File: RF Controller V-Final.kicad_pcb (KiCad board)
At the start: 2 copper layers, 132 x 67.5 mm, 41 parts, among them J2 J_OLED, J3 BAT+, J4 BAT-, SW1 EG1218, U1 Teensy4.0, U3 NRF24L01, U5 AP2112K-3.3, U7 Pitch/Roll, U8 TPS542025DDCR, U9 Throttle/Yaw

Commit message: Modified traces
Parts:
- moved U7 4.00 mm to (167.0, 131.0)
- moved U9 4.00 mm to (129.0, 105.0)
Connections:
- SW1 pad 1: /VBAT -> unconnected-(SW1-A-Pad1)
- SW1 pad 3: unconnected-(SW1-C-Pad3) -> /VBAT
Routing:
- net /3v3: track 57.0 -> 63.7 mm
- net /VBAT: track 8.74 -> 15.4 mm
- net /D9: track 47.0 -> 42.3 mm
- net /ADC3: track 65.9 -> 70.2 mm
- net /D10: track 52.3 -> 56.3 mm
- net /ADC0: track 59.1 -> 55.1 mm
- net /ADC1: track 59.9 -> 58.5 mm
- net /ADC2: track 77.9 -> 79.2 mm, vias 2 -> 4

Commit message: Added labels
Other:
- board text added: "5V"
- board text added: "GND"
- board text added: "SW"
- board text added: "VRx"
- board text added: "VRy"
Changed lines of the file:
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@@
+		)
+	)
+	(gr_text "VRx"
+		(at 137.5 118.5 0)
+		(layer "F.SilkS")
+		(effects
+			(font
+				(size 1 1)
+				(thickness 0.1)
+			)
+			(justify left bottom)
+		)
+	)
+	(gr_text "GND"
+		(at 137.5 123.5 0)
+		(layer "F.SilkS")
+		(effects
+			(font
+				(size 1 1)
+				(thickness 0.1)
+			)
+			(justify left bottom)
+		)
+	)
+	(gr_text "VRy"
+		(at 138 116 0)
+		(layer "F.SilkS")
+		(effects
+			(font
+				(size 1 1)
+				(thickness 0.1)
+			)
+			(justify left bottom)
+		)
+	)
+	(gr_text "SW"
+		(at 138.5 113.5 0)
+		(layer "F.SilkS")
+		(effects
+			(font
+				(size 1 1)
+				(thickness 0.1)
+			)
+			(justify left bottom)
+		)
+	)
+	(gr_text "5V"
+		(at 138.5 121 0)
+		(layer "F.SilkS")
+		(effects
+			(font
+				(size 1 1)
+				(thickness 0.1)
+			)
+			(justify left bottom)
+		)
+	)
+	(gr_text "GND"
+		(at 155.5 113.5 0)
+		(layer "F.SilkS")
+		(effects
+			(font
+				(size 1 1)
+				(thickness 0.1)
+			)
+			(justify left bottom)
+		)
+	)
+	(gr_text "5V"
+		(at 155.5 116 0)
+		(layer "F.SilkS")
+		(effects
+			(font
+				(size 1 1)
+				(thickness 0.1)
+			)
+			(justify left bottom)
+		)
+	)
+	(gr_text "VRx"
+		(at 155.5 118.5 0)
+		(layer "F.SilkS")
+		(effects
+			(font
+				(size 1 1)
+				(thickness 0.1)
+			)
+			(justify left bottom)
+		)
+	)
+	(gr_text "VRy"
+		(at 155.5 121 0)
+		(layer "F.SilkS")
+		(effects
+			(font
+				(size 1 1)
+				(thickness 0.1)
+			)
+			(justify left bottom)
+		)
+	)
+	(gr_text "SW"
+		(at 155.5 123.5 0)
+		(layer "F.SilkS")
+		(effects
+			(font
+				(size 1 1)
+				(thickness 0.1)
+			)
+			(justify left bottom)
 		)
 	)

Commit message: Made some design changes
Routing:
- net /D9: track 42.3 -> 43.0 mm, vias 1 -> 2
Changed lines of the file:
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@@
+	)
+	(segment
+		(start 140.039265 112.800735)
+		(end 141.730735 112.800735)
+		(width 0.2)
+		(layer "F.Cu")
+		(net "/D9")
 	)
 	(segment
@@
 	)
 	(segment
+		(start 141.730735 112.800735)
+		(end 141.85 112.92)
+		(width 0.2)
+		(layer "F.Cu")
+		(net "/D9")
+	)
+	(segment
 		(start 107 105.5)
 		(end 105.31 103.81)
@@
 		(net "/D9")
 	)
-	(segment
-		(start 114.42 112.92)
-		(end 141.08 112.92)
-		(width 0.2)
-		(layer "B.Cu")
+	(via
+		(at 140.039265 112.800735)
+		(size 0.6)
+		(drill 0.3)
+		(layers "F.Cu" "B.Cu")
 		(net "/D9")
 	)
 	(segment
+		(start 114 112.5)
+		(end 139.73853 112.5)
+		(width 0.2)
+		(layer "B.Cu")
+		(net "/D9")
+	)
+	(segment
 		(start 107 105.5)
-		(end 114.42 112.92)
+		(end 114 112.5)
+		(width 0.2)
+		(layer "B.Cu")
+		(net "/D9")
+	)
+	(segment
+		(start 139.73853 112.5)
+		(end 140.039265 112.800735)
 		(width 0.2)
 		(layer "B.Cu")
@@
 		(polygon
 			(pts
-				(xy 211.5 68) (xy 214 71) (xy 214 132.5) (xy 211 135.5) (xy 85 135.5) (xy 82 133.5) (xy 82 70.5)
-				(xy 85 68)
+				(xy 82 70.5) (xy 85 68) (xy 211.5 68) (xy 214 71) (xy 214 132.5) (xy 211.5 135.5) (xy 85 135.5)
+				(xy 82 133)
 			)
 		)

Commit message: Added dragon logo
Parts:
- removed the ? at (210.0, 72.0)
- removed the ? at (86.0, 131.5)
- removed the ? at (209.5, 132.0)
- removed the ? at (86.5, 71.5)
- added ?: LOGO, RF_MountingHoles:dragonart, F.Cu at (148.5, 101.0)

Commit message: Edited positions
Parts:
- moved U9 0.50 mm to (129.5, 105.0)
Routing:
- net /D9: track 43.0 -> 44.0 mm
- net /3v3: track 63.7 -> 63.2 mm
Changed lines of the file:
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@@
 	(footprint "JOYYFOOT:JOY1"
 		(layer "F.Cu")
-		(at 129 105 180)
+		(at 129.5 105 180)
 		(property "Reference" "U9"
 			(at 10.73 -10.66 180)
@@
 	)
 	(segment
-		(start 140.039265 112.800735)
-		(end 141.730735 112.800735)
+		(start 142.35 112.92)
+		(end 141.85 112.92)
+		(width 0.2)
+		(layer "F.Cu")
+		(net "/D9")
+	)
+	(segment
+		(start 142.230735 112.800735)
+		(end 142.35 112.92)
 		(width 0.2)
 		(layer "F.Cu")
@@
 	)
 	(segment
-		(start 141.730735 112.800735)
-		(end 141.85 112.92)
+		(start 140.039265 112.800735)
+		(end 142.230735 112.800735)
 		(width 0.2)
 		(layer "F.Cu")
@@
 	)
 	(segment
-		(start 151.55 114.06)
-		(end 145.07 120.54)
-		(width 0.8)
-		(layer "F.Cu")
-		(net "/3v3")
-	)
-	(segment
 		(start 151.55 111.1125)
 		(end 129.9375 89.5)
@@
 	)
 	(segment
-		(start 145.07 120.54)
-		(end 141.85 120.54)
+		(start 151.55 114.06)
+		(end 145.07 120.54)
 		(width 0.8)
 		(layer "F.Cu")
@@
 	)
 	(segment
+		(start 145.07 120.54)
+		(end 142.35 120.54)
+		(width 0.8)
+		(layer "F.Cu")
+		(net "/3v3")
+	)
+	(segment
 		(start 119.66 85.84)
 		(end 118.01 85.84)
@@
 	)
 	(segment
-		(start 128 118)
-		(end 141.85 118)
+		(start 114.31 87)
+		(end 112.754365 87)
 		(width 0.2)
 		(layer "F.Cu")
@@
 	)
 	(segment
-		(start 112.754365 87)
-		(end 114.31 87)
+		(start 111.83 87.924365)
+		(end 111.83 101.83)
 		(width 0.2)
 		(layer "F.Cu")
@@
 	)
 	(segment
-		(start 111.83 87.924365)
-		(end 112.754365 87)
+		(start 115.47 85.84)
+		(end 114.31 87)
 		(width 0.2)
 		(layer "F.Cu")
@@
 	)
 	(segment
-		(start 111.83 101.83)
-		(end 111.83 87.924365)
+		(start 128 118)
+		(end 142.35 118)
 		(width 0.2)
 		(layer "F.Cu")
@@
 	)
 	(segment
-		(start 114.31 87)
-		(end 115.47 85.84)
+		(start 112.754365 87)
+		(end 111.83 87.924365)
 		(width 0.2)
 		(layer "F.Cu")
@@
 	)
 	(segment
-		(start 128 118)
-		(end 111.83 101.83)
+		(start 111.83 101.83)
+		(end 128 118)
 		(width 0.2)
 		(layer "F.Cu")
@@
 	)
 	(segment
-		(start 116.57 85.384365)
-		(end 116.57 96.115635)
+		(start 127.711471 97.44)
+		(end 130.751471 94.4)
 		(width 0.2)
 		(layer "F.Cu")
@@
 	(segment
 		(start 139.1 112.71)
-		(end 141.85 115.46)
+		(end 141.545 115.155)
 		(width 0.2)
 		(layer "F.Cu")
@@
 	)
 	(segment
-		(start 114.03 84.74)
-		(end 115.925635 84.74)
+		(start 139.1 100.251471)
+		(end 139.1 112.71)
 		(width 0.2)
 		(layer "F.Cu")
@@
 	)
 	(segment
-		(start 141.85 115.155)
-		(end 141.85 115.46)
+		(start 141.545 115.155)
+		(end 141.85 115.155)
 		(width 0.2)
 		(layer "F.Cu")
@@
 	)
 	(segment
-		(start 117.894365 97.44)
-		(end 127.711471 97.44)
+		(start 133.248529 94.4)
+		(end 139.1 100.251471)
 		(width 0.2)
 		(layer "F.Cu")
@@
 	)
 	(segment
-		(start 116.57 96.115635)
-		(end 117.894365 97.44)
+		(start 114.03 84.74)
+		(end 115.925635 84.74)
 		(width 0.2)
 		(layer "F.Cu")
@@
 	)
 	(segment
-		(start 127.711471 97.44)
-		(end 130.751471 94.4)
+		(start 115.925635 84.74)
+		(end 116.57 85.384365)
 		(width 0.2)
 		(layer "F.Cu")
@@
 	)
 	(segment
-		(start 139.1 100.251471)
-		(end 139.1 112.71)
+		(start 116.57 85.384365)
+		(end 116.57 96.115635)
 		(width 0.2)
 		(layer "F.Cu")
@@
 	)
 	(segment
-		(start 115.925635 84.74)
-		(end 116.57 85.384365)
+		(start 117.894365 97.44)
+		(end 127.711471 97.44)
 		(width 0.2)
 		(layer "F.Cu")
@@
 	)
 	(segment
-		(start 133.248529 94.4)
-		(end 139.1 100.251471)
+		(start 116.57 96.115635)
+		(end 117.894365 97.44)
 		(width 0.2)
 		(layer "F.Cu")
@@
 	)
 	(segment
-		(start 129.734365 121.98)
-		(end 108.95 101.195635)
+		(start 107.85 85.84)
+		(end 108.95 86.94)
 		(width 0.2)
 		(layer "F.Cu")
@@
 	)
 	(segment
-		(start 154.15 120.54)
-		(end 150.15 120.54)
+		(start 108.95 86.94)
+		(end 108.95 101.195635)
 		(width 0.2)
 		(layer "F.Cu")
@@
 	)
 	(segment
-		(start 142.97 122)
-		(end 142.95 121.98)
+		(start 150.15 120.54)
+		(end 154.15 120.54)
 		(width 0.2)
 		(layer "F.Cu")
@@
 	)
 	(segment
-		(start 108.95 86.94)
-		(end 107.85 85.84)
+		(start 130.474365 121.64)
+		(end 149.05 121.64)
 		(width 0.2)
 		(layer "F.Cu")
@@
 	)
 	(segment
-		(start 150.15 120.54)
-		(end 148.69 122)
+		(start 129.754365 122)
+		(end 130.114365 122)
 		(width 0.2)
 		(layer "F.Cu")
@@
 	)
 	(segment
-		(start 142.95 121.98)
-		(end 129.734365 121.98)
+		(start 149.05 121.64)
+		(end 150.15 120.54)
 		(width 0.2)
 		(layer "F.Cu")
@@
 	(segment
 		(start 108.95 101.195635)
-		(end 108.95 86.94)
+		(end 129.754365 122)
 		(width 0.2)
 		(layer "F.Cu")
@@
 	)
 	(segment
-		(start 148.69 122)
-		(end 142.97 122)
+		(start 130.114365 122)
+		(end 130.474365 121.64)
 		(width 0.2)
 		(layer "F.Cu")
@@
 		(polygon
 			(pts
-				(xy 82 70.5) (xy 85 68) (xy 211.5 68) (xy 214 71) (xy 214 132.5) (xy 211.5 135.5) (xy 85 135.5)
-				(xy 82 133)
+				(xy 82 70.5) (xy 85 68) (xy 211.5 68) (xy 214 71) (xy 214 133) (xy 211.5 135.5) (xy 85.5 135.5)
+				(xy 82 132.5)
 			)
 		)

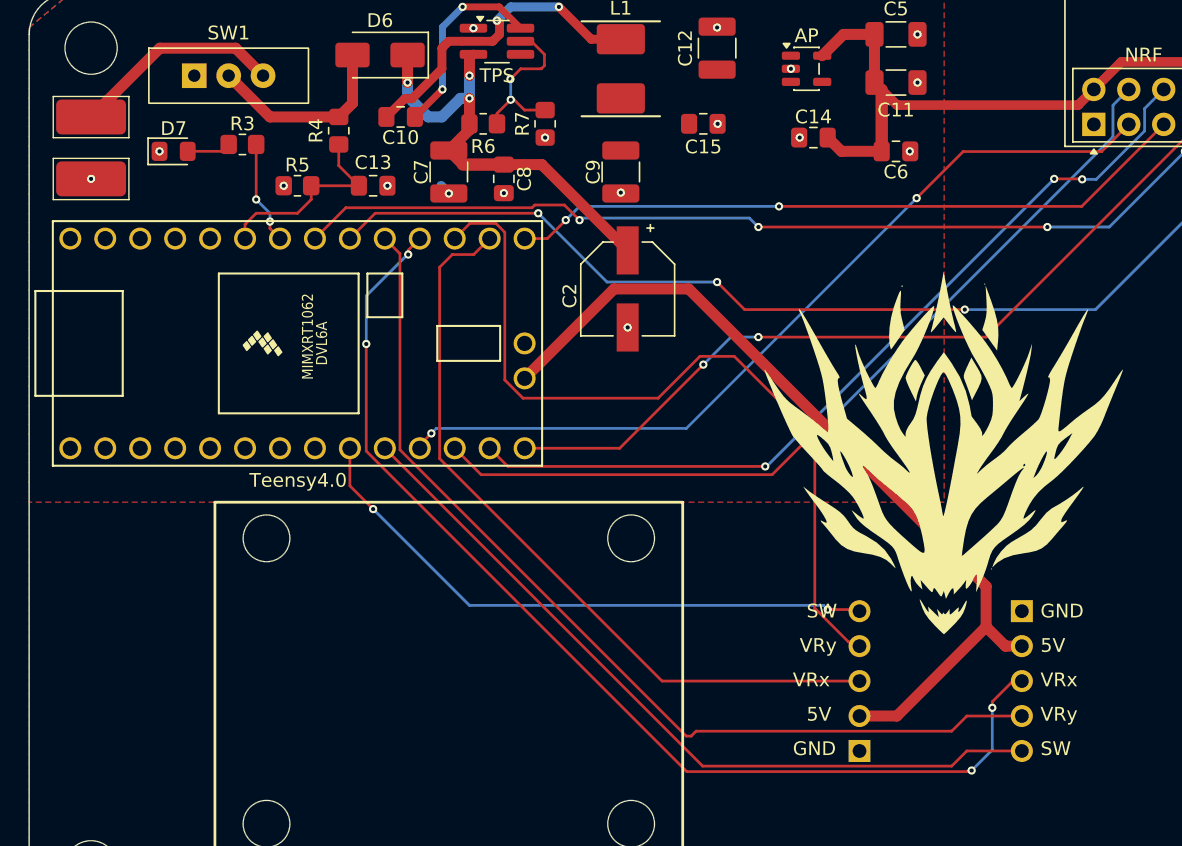
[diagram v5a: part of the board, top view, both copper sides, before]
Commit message: Modified silkscreen
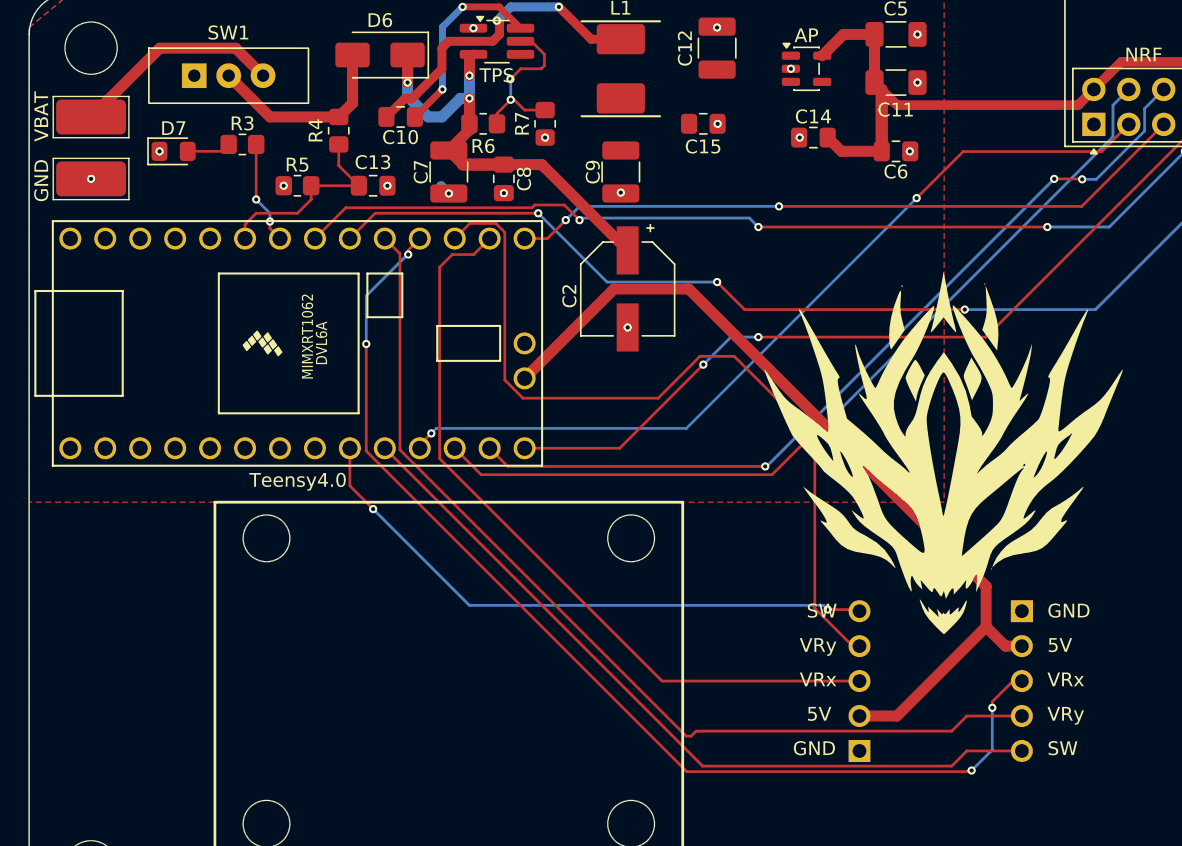
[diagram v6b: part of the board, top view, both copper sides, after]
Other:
- board text added: "VBAT"
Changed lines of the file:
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@@
-		)
-	)
-	(gr_text "VRx"
-		(at 137.5 118.5 0)
-		(layer "F.SilkS")
-		(effects
-			(font
-				(size 1 1)
-				(thickness 0.1)
-			)
-			(justify left bottom)
 		)
 	)
@@
 	(gr_text "VRy"
 		(at 138 116 0)
+		(layer "F.SilkS")
+		(effects
+			(font
+				(size 1 1)
+				(thickness 0.1)
+			)
+			(justify left bottom)
+		)
+	)
+	(gr_text "VRx"
+		(at 138 118.5 0)
 		(layer "F.SilkS")
 		(effects
@@
 	)
 	(gr_text "GND"
-		(at 155.5 113.5 0)
+		(at 156 113.5 0)
 		(layer "F.SilkS")
 		(effects
@@
 	)
 	(gr_text "5V"
-		(at 155.5 116 0)
+		(at 156 116 0)
 		(layer "F.SilkS")
 		(effects
@@
 	)
 	(gr_text "VRx"
-		(at 155.5 118.5 0)
+		(at 156 118.5 0)
 		(layer "F.SilkS")
 		(effects
@@
 	)
 	(gr_text "VRy"
-		(at 155.5 121 0)
+		(at 156 121 0)
 		(layer "F.SilkS")
 		(effects
@@
 	)
 	(gr_text "SW"
-		(at 155.5 123.5 0)
+		(at 156 123.5 0)
 		(layer "F.SilkS")
 		(effects
@@
 		(layer "F.SilkS")
 		(effects
+			(font
+				(size 1 1)
+				(thickness 0.1)
+			)
+			(justify left bottom)
+		)
+	)
+	(gr_text "VBAT"
+		(at 83.5 78.8 90)
+		(layer "F.SilkS")
+		(effects
+			(font
+				(size 1 1)
+				(thickness 0.1)
+			)
+			(justify left bottom)
+		)
+	)
+	(gr_text "GND"
+		(at 83.5 83.2 90)
+		(layer "F.SilkS")
+		(effects
